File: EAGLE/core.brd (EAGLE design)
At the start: 20.3 x 35.6 mm, 47 parts, among them IC1 MCP1825S-3302E, Q1 MMDT3904, U2 STM32F10XCXT6, U3 SST25VF040B-S2, X1 USB-MICROB, X2 IPEX-20279-001E, Y1 32Khz, Y2 8Mhz

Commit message: 0402 components
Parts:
- C3, C6: device rcl:C0603 -> SparkFun-Capacitors:0402-CAP
- L1, L3: device SparkFun-Passives:0603 -> SparkFun-Passives:C0402
- moved ANT1 1.91 mm to (9.14, 1.02)
- moved L3 1.17 mm to (13.8, 3.17)
- moved C3 0.63 mm to (13.2, 4.75)
- moved L1 0.36 mm to (13.8, 6.48)
- moved C6 0.28 mm to (12.5, 5.36)
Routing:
- net N$3: track 3.68 -> 3.11 mm
- net GND: vias 19 -> 16
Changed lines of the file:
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@@
 <plain>
 <wire x1="0" y1="35.56" x2="0" y2="2.54" width="0.2032" layer="20"/>
-<wire x1="0" y1="2.54" x2="2.54" y2="0" width="0.2032" layer="20"/>
 <wire x1="2.54" y1="0" x2="17.78" y2="0" width="0.2032" layer="20"/>
 <wire x1="17.78" y1="0" x2="20.32" y2="2.54" width="0.2032" layer="20"/>
@@
 </element>
 <element name="U1" library="CC3000" package="CC3000" value="" x="10.16" y="15.24" locked="yes" smashed="yes" rot="R180"/>
-<element name="L1" library="SparkFun-Passives" package="0603" value="2.2nH" x="14.097" y="6.223" smashed="yes">
-<attribute name="NAME" x="13.208" y="6.985" size="0.4064" layer="25" font="vector"/>
-<attribute name="VALUE" x="15.621" y="7.366" size="0.4064" layer="27" font="vector" rot="R270"/>
-</element>
-<element name="C3" library="rcl" package="C0603" value="2.2pF" x="13.208" y="4.1148" smashed="yes" rot="R90">
-<attribute name="NAME" x="12.573" y="3.4798" size="1.27" layer="25" rot="R90"/>
-<attribute name="VALUE" x="12.573" y="3.6322" size="0.4064" layer="27" rot="R180"/>
+<element name="L1" library="SparkFun-Passives" package="C0402" value="2.2nH" x="13.843" y="6.477" smashed="yes">
+<attribute name="NAME" x="12.954" y="7.239" size="0.4064" layer="25" font="vector"/>
+<attribute name="VALUE" x="15.367" y="7.62" size="0.4064" layer="27" font="vector" rot="R270"/>
+</element>
+<element name="C3" library="SparkFun-Capacitors" package="0402-CAP" value="2.2pF" x="13.208" y="4.7498" smashed="yes" rot="R90">
+<attribute name="NAME" x="12.573" y="4.1148" size="1.27" layer="25" rot="R90"/>
+<attribute name="VALUE" x="12.573" y="4.2672" size="0.4064" layer="27" rot="R180"/>
 </element>
 <element name="C4" library="rcl" package="C0603" value="100nF" x="5.969" y="24.257" locked="yes" smashed="yes">
@@
 </element>
 <element name="X2" library="Spark" package="IPEX-20279-001E" value="IPEX-20279-001E" x="5.08" y="4.318" locked="yes"/>
-<element name="C6" library="rcl" package="C0603" value="10pF" x="12.3444" y="5.1054" smashed="yes" rot="R180">
-<attribute name="NAME" x="12.9794" y="4.4704" size="1.27" layer="25" rot="R180"/>
-<attribute name="VALUE" x="10.6934" y="5.2324" size="0.4064" layer="27" rot="R180"/>
-</element>
-<element name="ANT1" library="Spark" package="AT8010" value="AT8010" x="7.239" y="1.016" smashed="yes">
-<attribute name="NAME" x="3.249" y="1.706" size="0.4064" layer="25"/>
+<element name="C6" library="SparkFun-Capacitors" package="0402-CAP" value="10pF" x="12.4714" y="5.3594" smashed="yes" rot="R180">
+<attribute name="NAME" x="13.1064" y="4.7244" size="1.27" layer="25" rot="R180"/>
+<attribute name="VALUE" x="10.8204" y="5.4864" size="0.4064" layer="27" rot="R180"/>
+</element>
+<element name="ANT1" library="Spark" package="AT8010" value="AT8010" x="9.144" y="1.016" smashed="yes">
+<attribute name="NAME" x="5.154" y="1.706" size="0.4064" layer="25"/>
 </element>
 <element name="C16" library="Spark" package="EIA3216" value="10uF" x="16.383" y="34.29" locked="yes" smashed="yes" rot="MR180">
@@
 </element>
 <element name="D1" library="Spark" package="DIODE-DO-220AA(SMP)" value="DIODE" x="3.048" y="34.036" locked="yes"/>
-<element name="L3" library="SparkFun-Passives" package="0603" value="2.2nH" x="14.097" y="2.032"/>
+<element name="L3" library="SparkFun-Passives" package="C0402" value="2.2nH" x="13.843" y="3.175"/>
 </elements>
 <signals>
@@
 <via x="0.762" y="33.528" extent="1-16" drill="0.3"/>
 <contactref element="L3" pad="2"/>
-<polygon width="0.1524" layer="1" thermals="no">
-<vertex x="12.192" y="3.302"/>
-<vertex x="12.192" y="0.254"/>
-<vertex x="17.272" y="0.254"/>
-<vertex x="17.272" y="0.381"/>
-<vertex x="17.272" y="3.429"/>
-<vertex x="12.192" y="3.429"/>
-</polygon>
-<via x="15.113" y="0.889" extent="1-16" drill="0.3"/>
-<via x="15.113" y="3.302" extent="1-16" drill="0.3"/>
-<via x="15.113" y="4.953" extent="1-16" drill="0.3"/>
+<wire x1="11.43" y1="3.81" x2="14.493" y2="3.175" width="0" layer="19" extent="1-1"/>
 </signal>
 <signal name="RAW" class="1">
@@
 <wire x1="5.3975" y1="6.3754" x2="5.08" y2="6.0579" width="0.635" layer="1"/>
 <wire x1="5.08" y1="6.0579" x2="5.08" y2="5.8455" width="0.635" layer="1"/>
-<wire x1="8.7376" y1="6.3754" x2="10.0076" y2="5.1054" width="0.635" layer="1"/>
-<wire x1="10.0076" y1="5.1054" x2="11.4944" y2="5.1054" width="0.635" layer="1"/>
+<wire x1="8.7376" y1="6.3754" x2="9.7536" y2="5.3594" width="0.635" layer="1"/>
+<wire x1="9.7536" y1="5.3594" x2="11.8214" y2="5.3594" width="0.635" layer="1"/>
 </signal>
 <signal name="N$3" class="2">
@@
 <contactref element="C3" pad="1"/>
 <contactref element="L3" pad="1"/>
-<wire x1="13.208" y1="3.2648" x2="13.208" y2="2.071" width="0.635" layer="1"/>
-<wire x1="13.208" y1="2.071" x2="13.247" y2="2.032" width="0.635" layer="1"/>
-<wire x1="13.247" y1="2.032" x2="12.231" y2="1.016" width="0.635" layer="1" curve="-90"/>
-<wire x1="12.231" y1="1.016" x2="11.239" y2="1.016" width="0.635" layer="1"/>
+<wire x1="13.208" y1="4.0998" x2="13.208" y2="3.19" width="0.635" layer="1"/>
+<wire x1="13.208" y1="3.19" x2="13.193" y2="3.175" width="0.635" layer="1"/>
+<wire x1="13.193" y1="3.175" x2="13.193" y2="1.065" width="0.635" layer="1"/>
+<wire x1="13.193" y1="1.065" x2="13.144" y2="1.016" width="0.635" layer="1"/>
 </signal>
 <signal name="N$5" class="2">
@@
 <contactref element="U1" pad="RF_ANT"/>
 <contactref element="C6" pad="1"/>
-<wire x1="13.16" y1="7.96" x2="13.16" y2="6.31" width="0.635" layer="1"/>
-<wire x1="13.16" y1="6.31" x2="13.247" y2="6.223" width="0.635" layer="1"/>
-<wire x1="13.247" y1="6.223" x2="13.247" y2="5.158" width="0.635" layer="1"/>
-<wire x1="13.247" y1="5.158" x2="13.1944" y2="5.1054" width="0.635" layer="1"/>
-<wire x1="13.208" y1="4.9648" x2="13.1944" y2="5.1054" width="0" layer="19" extent="1-1"/>
+<wire x1="13.16" y1="7.96" x2="13.16" y2="6.51" width="0.635" layer="1"/>
+<wire x1="13.16" y1="6.51" x2="13.193" y2="6.477" width="0.635" layer="1"/>
+<wire x1="13.193" y1="6.477" x2="13.193" y2="5.4148" width="0.635" layer="1"/>
+<wire x1="13.193" y1="5.4148" x2="13.208" y2="5.3998" width="0.635" layer="1"/>
+<wire x1="13.208" y1="5.3998" x2="13.1618" y2="5.3998" width="0.635" layer="1"/>
+<wire x1="13.1618" y1="5.3998" x2="13.1214" y2="5.3594" width="0.635" layer="1"/>
 </signal>
 <signal name="LED1">

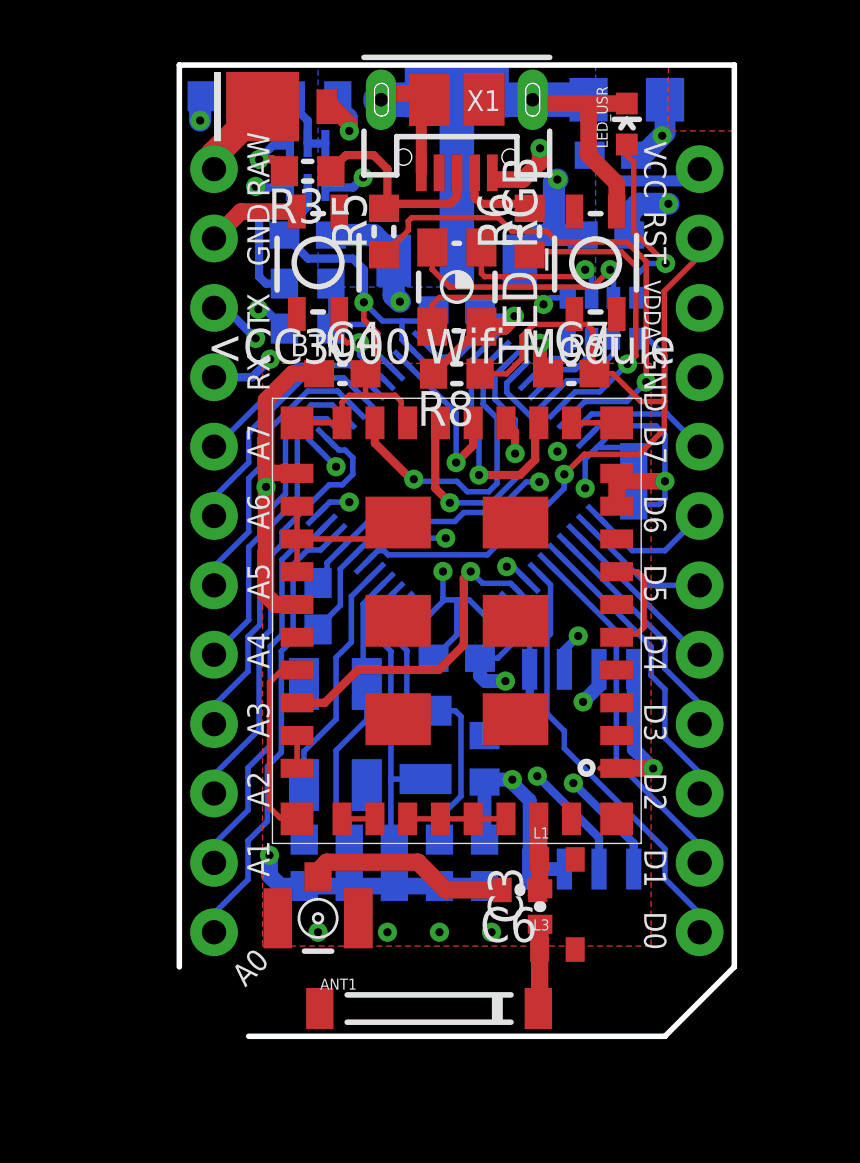
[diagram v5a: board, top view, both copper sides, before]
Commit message: Clean RF circuit with 0603
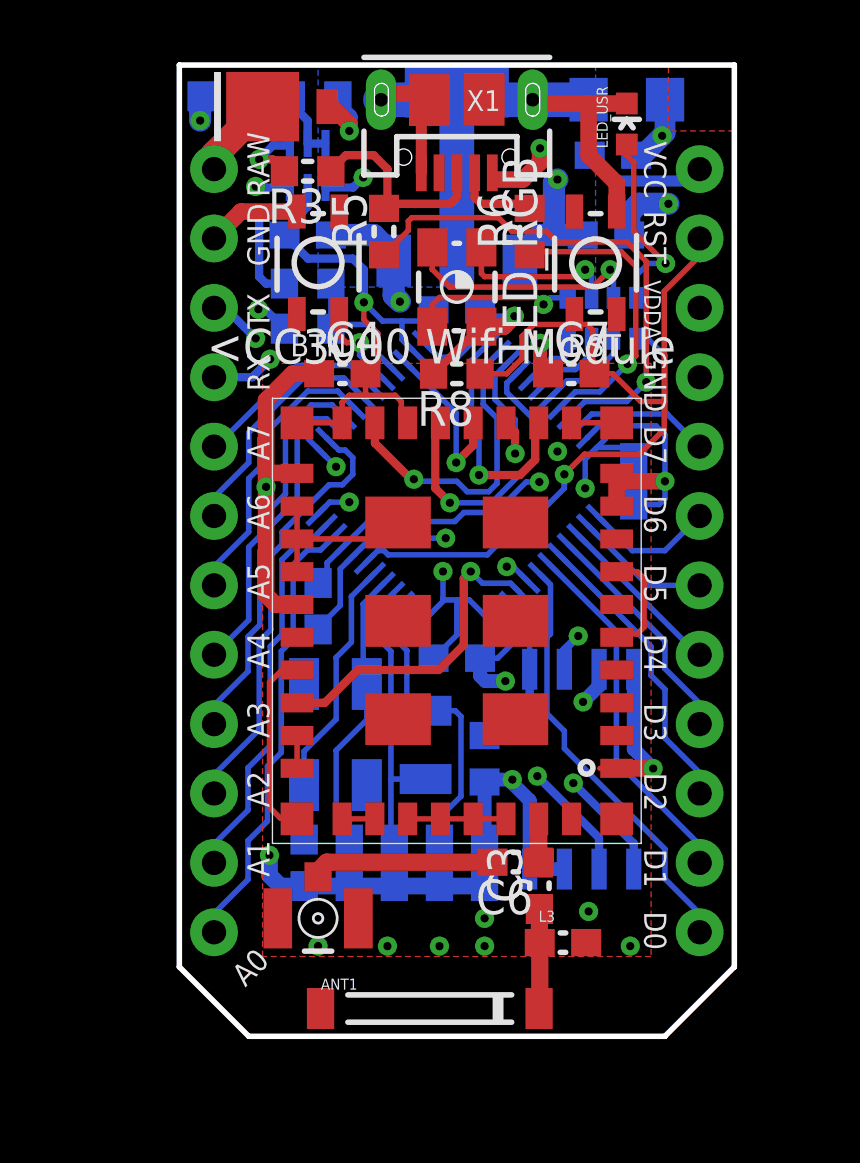
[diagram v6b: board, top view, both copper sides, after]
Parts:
- removed L1: 2.2nH, SparkFun-Passives:C0402
- C3, C6: device SparkFun-Capacitors:0402-CAP -> rcl:C0603
- L3: device SparkFun-Passives:C0402 -> SparkFun-Passives:0603
- moved C6 1.03 mm to (12.3, 6.38)
- moved C3 0.76 mm to (13.2, 5.51)
- moved L3 0.33 mm to (14.0, 3.43)
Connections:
- net GND: no longer L1.2
- net N$5: no longer L1.1
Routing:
- net N$5: track 2.68 -> 1.61 mm
- net N$2: track 7.51 -> 6.73 mm
- net N$3: track 3.11 -> 3.66 mm
- net GND: vias 16 -> 19
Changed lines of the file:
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@@
 <plain>
 <wire x1="0" y1="35.56" x2="0" y2="2.54" width="0.2032" layer="20"/>
+<wire x1="0" y1="2.54" x2="2.54" y2="0" width="0.2032" layer="20"/>
 <wire x1="2.54" y1="0" x2="17.78" y2="0" width="0.2032" layer="20"/>
 <wire x1="17.78" y1="0" x2="20.32" y2="2.54" width="0.2032" layer="20"/>
@@
 </element>
 <element name="U1" library="CC3000" package="CC3000" value="" x="10.16" y="15.24" locked="yes" smashed="yes" rot="R180"/>
-<element name="L1" library="SparkFun-Passives" package="C0402" value="2.2nH" x="13.843" y="6.477" smashed="yes">
-<attribute name="NAME" x="12.954" y="7.239" size="0.4064" layer="25" font="vector"/>
-<attribute name="VALUE" x="15.367" y="7.62" size="0.4064" layer="27" font="vector" rot="R270"/>
-</element>
-<element name="C3" library="SparkFun-Capacitors" package="0402-CAP" value="2.2pF" x="13.208" y="4.7498" smashed="yes" rot="R90">
-<attribute name="NAME" x="12.573" y="4.1148" size="1.27" layer="25" rot="R90"/>
-<attribute name="VALUE" x="12.573" y="4.2672" size="0.4064" layer="27" rot="R180"/>
+<element name="C3" library="rcl" package="C0603" value="2.2pF" x="13.1826" y="5.5118" smashed="yes" rot="R90">
+<attribute name="NAME" x="12.5476" y="4.8768" size="1.27" layer="25" rot="R90"/>
+<attribute name="VALUE" x="12.5476" y="5.0292" size="0.4064" layer="27" rot="R180"/>
 </element>
 <element name="C4" library="rcl" package="C0603" value="100nF" x="5.969" y="24.257" locked="yes" smashed="yes">
@@
 </element>
 <element name="X2" library="Spark" package="IPEX-20279-001E" value="IPEX-20279-001E" x="5.08" y="4.318" locked="yes"/>
-<element name="C6" library="SparkFun-Capacitors" package="0402-CAP" value="10pF" x="12.4714" y="5.3594" smashed="yes" rot="R180">
-<attribute name="NAME" x="13.1064" y="4.7244" size="1.27" layer="25" rot="R180"/>
-<attribute name="VALUE" x="10.8204" y="5.4864" size="0.4064" layer="27" rot="R180"/>
-</element>
-<element name="ANT1" library="Spark" package="AT8010" value="AT8010" x="9.144" y="1.016" smashed="yes">
-<attribute name="NAME" x="5.154" y="1.706" size="0.4064" layer="25"/>
+<element name="C6" library="rcl" package="C0603" value="10pF" x="12.319" y="6.3754" smashed="yes" rot="R180">
+<attribute name="NAME" x="12.954" y="5.7404" size="1.27" layer="25" rot="R180"/>
+<attribute name="VALUE" x="10.668" y="6.5024" size="0.4064" layer="27" rot="R180"/>
+</element>
+<element name="ANT1" library="Spark" package="AT8010" value="AT8010" x="9.1694" y="1.016" smashed="yes">
+<attribute name="NAME" x="5.1794" y="1.706" size="0.4064" layer="25"/>
 </element>
 <element name="C16" library="Spark" package="EIA3216" value="10uF" x="16.383" y="34.29" locked="yes" smashed="yes" rot="MR180">
@@
 </element>
 <element name="D1" library="Spark" package="DIODE-DO-220AA(SMP)" value="DIODE" x="3.048" y="34.036" locked="yes"/>
-<element name="L3" library="SparkFun-Passives" package="C0402" value="2.2nH" x="13.843" y="3.175"/>
+<element name="L3" library="SparkFun-Passives" package="0603" value="2.2nH" x="14.0462" y="3.429"/>
 </elements>
 <signals>
@@
 <contactref element="C15" pad="2"/>
 <contactref element="U1" pad="GND@36"/>
-<contactref element="L1" pad="2"/>
 <contactref element="U1" pad="GND@31"/>
 <contactref element="U1" pad="GND@32"/>
@@
 <vertex x="0" y="35.56"/>
 <vertex x="20.32" y="35.56"/>
-<vertex x="20.32" y="3.302"/>
-<vertex x="0" y="3.302"/>
+<vertex x="20.447" y="2.921"/>
+<vertex x="0.127" y="2.921"/>
 </polygon>
 <contactref element="U1" pad="GND@39"/>
@@
 <contactref element="X2" pad="2@1"/>
 <contactref element="X2" pad="2@2"/>
-<via x="5.08" y="3.81" extent="1-16" drill="0.3"/>
-<via x="7.62" y="3.81" extent="1-16" drill="0.3"/>
-<via x="9.525" y="3.81" extent="1-16" drill="0.3"/>
-<via x="11.43" y="3.81" extent="1-16" drill="0.3"/>
+<via x="5.08" y="3.302" extent="1-16" drill="0.3"/>
+<via x="7.62" y="3.302" extent="1-16" drill="0.3"/>
+<via x="9.525" y="3.302" extent="1-16" drill="0.3"/>
+<via x="11.176" y="3.302" extent="1-16" drill="0.3"/>
 <polygon width="0.1524" layer="1" thermals="no">
-<vertex x="3.048" y="3.302"/>
+<vertex x="3.048" y="2.921"/>
 <vertex x="3.048" y="24.638"/>
 <vertex x="17.272" y="24.638"/>
-<vertex x="17.272" y="3.302"/>
+<vertex x="17.272" y="2.921"/>
 </polygon>
 <contactref element="C16" pad="C"/>
@@
 <via x="0.762" y="33.528" extent="1-16" drill="0.3"/>
 <contactref element="L3" pad="2"/>
-<wire x1="11.43" y1="3.81" x2="14.493" y2="3.175" width="0" layer="19" extent="1-1"/>
+<via x="16.51" y="3.302" extent="1-16" drill="0.3"/>
+<via x="11.176" y="4.318" extent="1-16" drill="0.3"/>
+<via x="14.986" y="4.572" extent="1-16" drill="0.3"/>
 </signal>
 <signal name="RAW" class="1">
@@
 <contactref element="C6" pad="2"/>
 <contactref element="X2" pad="1"/>
-<wire x1="8.7376" y1="6.3754" x2="5.3975" y2="6.3754" width="0.635" layer="1"/>
 <wire x1="5.3975" y1="6.3754" x2="5.08" y2="6.0579" width="0.635" layer="1"/>
 <wire x1="5.08" y1="6.0579" x2="5.08" y2="5.8455" width="0.635" layer="1"/>
-<wire x1="8.7376" y1="6.3754" x2="9.7536" y2="5.3594" width="0.635" layer="1"/>
-<wire x1="9.7536" y1="5.3594" x2="11.8214" y2="5.3594" width="0.635" layer="1"/>
+<wire x1="11.469" y1="6.3754" x2="5.3975" y2="6.3754" width="0.635" layer="1"/>
 </signal>
 <signal name="N$3" class="2">
@@
 <contactref element="C3" pad="1"/>
 <contactref element="L3" pad="1"/>
-<wire x1="13.208" y1="4.0998" x2="13.208" y2="3.19" width="0.635" layer="1"/>
-<wire x1="13.208" y1="3.19" x2="13.193" y2="3.175" width="0.635" layer="1"/>
-<wire x1="13.193" y1="3.175" x2="13.193" y2="1.065" width="0.635" layer="1"/>
-<wire x1="13.193" y1="1.065" x2="13.144" y2="1.016" width="0.635" layer="1"/>
+<wire x1="13.1826" y1="4.6618" x2="13.1826" y2="3.4426" width="0.635" layer="1"/>
+<wire x1="13.1826" y1="3.4426" x2="13.1962" y2="3.429" width="0.635" layer="1"/>
+<wire x1="13.1962" y1="3.429" x2="13.1962" y2="1.0428" width="0.635" layer="1"/>
+<wire x1="13.1962" y1="1.0428" x2="13.1694" y2="1.016" width="0.635" layer="1"/>
 </signal>
 <signal name="N$5" class="2">
 <contactref element="C3" pad="2"/>
-<contactref element="L1" pad="1"/>
 <contactref element="U1" pad="RF_ANT"/>
 <contactref element="C6" pad="1"/>
-<wire x1="13.16" y1="7.96" x2="13.16" y2="6.51" width="0.635" layer="1"/>
-<wire x1="13.16" y1="6.51" x2="13.193" y2="6.477" width="0.635" layer="1"/>
-<wire x1="13.193" y1="6.477" x2="13.193" y2="5.4148" width="0.635" layer="1"/>
-<wire x1="13.193" y1="5.4148" x2="13.208" y2="5.3998" width="0.635" layer="1"/>
-<wire x1="13.208" y1="5.3998" x2="13.1618" y2="5.3998" width="0.635" layer="1"/>
-<wire x1="13.1618" y1="5.3998" x2="13.1214" y2="5.3594" width="0.635" layer="1"/>
+<wire x1="13.1826" y1="6.3618" x2="13.169" y2="6.3754" width="0.635" layer="1"/>
+<wire x1="13.16" y1="7.96" x2="13.16" y2="6.3844" width="0.635" layer="1"/>
+<wire x1="13.16" y1="6.3844" x2="13.169" y2="6.3754" width="0.635" layer="1"/>
 </signal>
 <signal name="LED1">

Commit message: Renumbered components
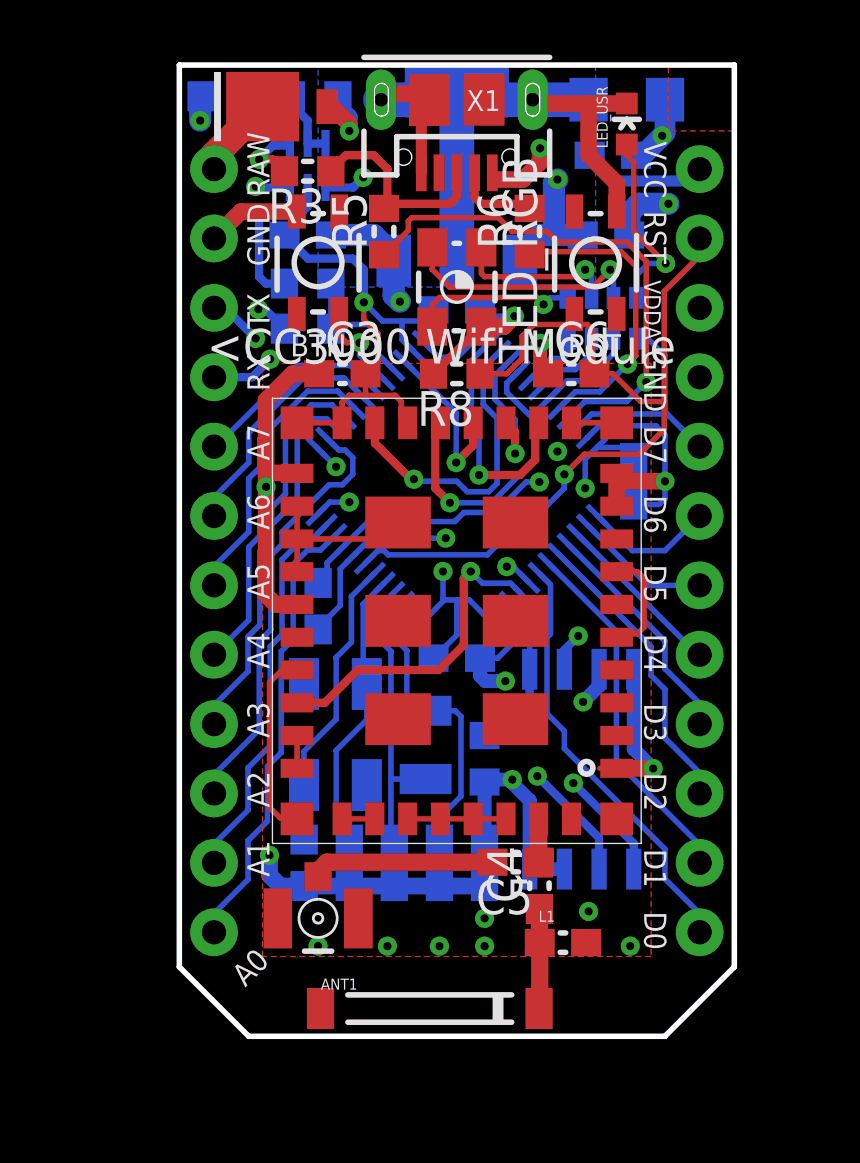
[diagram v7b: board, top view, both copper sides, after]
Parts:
- removed C17: 100nF, rcl:C0603
- added C5: 10pF, rcl:C0603
- C12: value 22pF -> 100nF
- C15: value 100nF -> 10uF; device rcl:C0603 -> Spark:EIA3216
- C16: value 10uF -> 100nF; device Spark:EIA3216 -> rcl:C0603
- C3: value 2.2pF -> 100nF
- C4: value 100nF -> 2.2pF
- C6: value 10pF -> 100nF
- C8: value 100nF -> 22pF
- moved C15 21.4 mm to (16.4, 34.3)
- moved C12 20.6 mm to (10.2, 26.6), turned to 0 degrees
- moved C3 20.1 mm to (5.97, 24.3), turned to 0 degrees
- moved C4 20.1 mm to (13.2, 5.51), turned to 90 degrees
- moved C7 18.2 mm to (11.2, 6.35), flipped to the bottom, turned to 270 degrees
- moved C6 18.0 mm to (14.4, 24.3), turned to 0 degrees
- moved C16 14.0 mm to (16.6, 20.3), turned to 270 degrees
- moved C13 12.0 mm to (5.08, 15.7), turned to 270 degrees
- moved C14 5.43 mm to (10.2, 13.8), turned to 180 degrees
- moved C10 4.95 mm to (4.57, 6.35)
- moved C8 3.30 mm to (7.87, 6.35)
- moved C9 1.65 mm to (9.53, 6.35)
- moved C11 1.65 mm to (6.22, 6.35)
- renumbered L3 to L1
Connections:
- net !RST: now also C6.2; no longer C7.2
- net +3V3: now also C12.1, C14.1, C16.1, C3.1, C7.1; no longer C13.1, C15.1, C17.1, C4.1, C8.1
- net GND: now also C15.C, C16.2, C3.2, C6.1, C7.2; no longer C15.2, C16.C, C17.2, C4.2, C7.1
- net N$2: now also C5.2; no longer C6.2
- net N$3: now also C4.1; no longer C3.1
- net N$5: now also C4.2, C5.1; no longer C3.2, C6.1
- net OSC32_IN: now also C9.1; no longer C10.1
- net OSC32_OUT: now also C8.1; no longer C9.1
- net OSC_IN: now also C11.1; no longer C12.1
- net OSC_OUT: now also C10.1; no longer C11.1
- net VDDA: now also C13.1, C15.A; no longer C14.1, C16.A

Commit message: Fixed up BoM
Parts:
- C8, C9: value 22pF -> 10pF
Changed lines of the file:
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@@
 <attribute name="NAME" x="11.684" y="13.589" size="1.016" layer="26" rot="MR270"/>
 </element>
-<element name="C8" library="rcl" package="C0603" value="22pF" x="7.874" y="6.35" locked="yes" smashed="yes" rot="MR270">
+<element name="C8" library="rcl" package="C0603" value="10pF" x="7.874" y="6.35" locked="yes" smashed="yes" rot="MR270">
 <attribute name="NAME" x="7.239" y="6.985" size="1.27" layer="26" rot="MR270"/>
 <attribute name="VALUE" x="8.128" y="4.826" size="0.6096" layer="28" rot="MR270"/>
 </element>
-<element name="C9" library="rcl" package="C0603" value="22pF" x="9.525" y="6.35" locked="yes" smashed="yes" rot="MR270">
+<element name="C9" library="rcl" package="C0603" value="10pF" x="9.525" y="6.35" locked="yes" smashed="yes" rot="MR270">
 <attribute name="NAME" x="8.89" y="6.985" size="1.27" layer="26" rot="MR270"/>
 <attribute name="VALUE" x="9.779" y="4.826" size="0.6096" layer="28" rot="MR270"/>
